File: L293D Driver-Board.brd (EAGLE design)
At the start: 62.2 x 47.9 mm, 13 parts, among them IC1 L293D, IC3 LM317MBSTT3

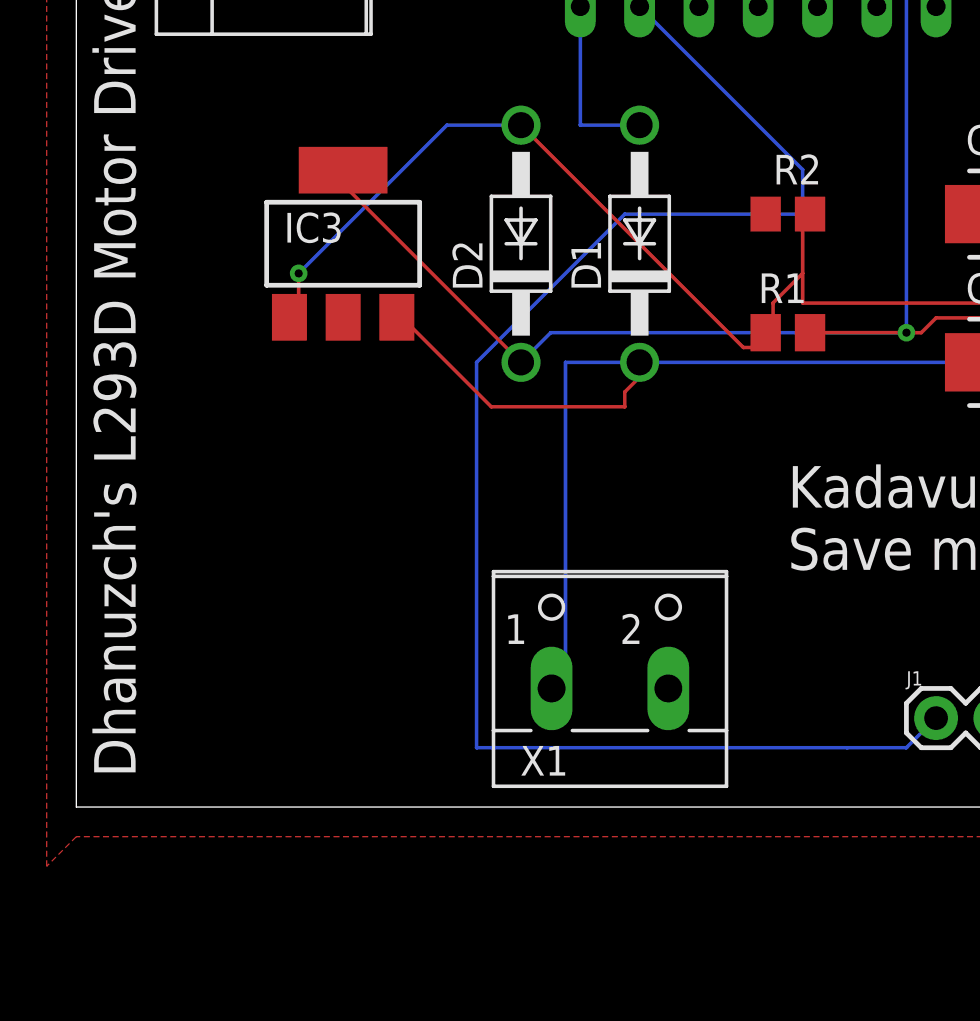
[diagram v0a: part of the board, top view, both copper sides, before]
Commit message: Changed Resistor Values
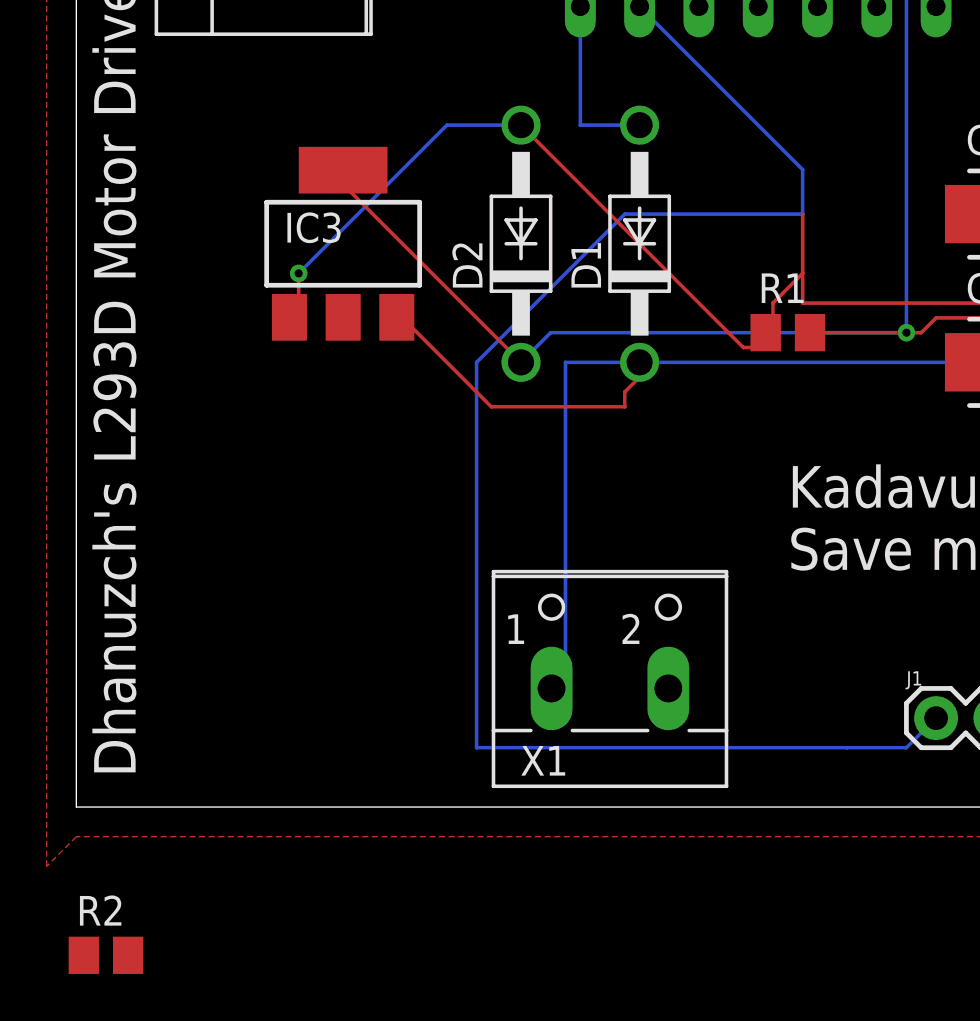
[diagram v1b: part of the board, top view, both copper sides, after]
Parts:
- R2: value (none) -> 720Ω; device designblock:R0805 -> resistor:M0805
- moved R2 43.1 mm to (1.27, -6.35)
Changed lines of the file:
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@@
 <attribute name="VALUE" x="29.21" y="17.78" size="1.27" layer="27"/>
-</element>
-<element name="R2" library="designblock" package="R0805" value="" x="30.48" y="25.4" smashed="yes">
-<attribute name="NAME" x="29.845" y="26.67" size="1.27" layer="25"/>
-<attribute name="VALUE" x="29.845" y="22.86" size="1.27" layer="27"/>
 </element>
 <element name="X1" library="con-wago-500" library_urn="urn:adsk.eagle:library:195" package="W237-102" package3d_urn="urn:adsk.eagle:package:10688/1" value="" x="22.86" y="6.35" smashed="yes">
@@
 <attribute name="VALUE" x="1.27" y="43.14" size="1.27" layer="27" ratio="10" rot="R270"/>
 </element>
+<element name="R2" library="resistor" library_urn="urn:adsk.eagle:library:348" package="M0805" package3d_urn="urn:adsk.eagle:package:26079/1" value="720Ω" x="1.27" y="-6.35" smashed="yes">
+<attribute name="NAME" x="0" y="-5.08" size="1.27" layer="25"/>
+<attribute name="VALUE" x="0" y="-8.89" size="1.27" layer="27"/>
+</element>
 </elements>
 <signals>
@@
 <contactref element="C3" pad="2"/>
 <contactref element="X1" pad="2"/>
-<contactref element="R2" pad="1"/>
 <contactref element="C5" pad="-"/>
 <contactref element="C4" pad="-"/>
@@
 <vertex x="-1.27" y="48.26"/>
 </polygon>
+<contactref element="R2" pad="1"/>
+<wire x1="38.66" y1="25.4" x2="52.07" y2="26.67" width="0" layer="19" extent="1-1"/>
+<wire x1="38.66" y1="19.05" x2="38.66" y2="25.4" width="0" layer="19" extent="1-1"/>
+<wire x1="31.75" y1="34.29" x2="38.66" y2="25.4" width="0" layer="19" extent="1-1"/>
+<wire x1="29.21" y1="34.29" x2="31.75" y2="34.29" width="0" layer="19" extent="1-1"/>
+<wire x1="31.75" y1="41.91" x2="31.75" y2="34.29" width="0" layer="19" extent="1-1"/>
+<wire x1="29.21" y1="41.91" x2="31.75" y2="41.91" width="0" layer="19" extent="1-1"/>
+<wire x1="25.36" y1="5.08" x2="38.66" y2="19.05" width="0" layer="19" extent="1-1"/>
+<wire x1="0.32" y1="-6.35" x2="25.36" y2="5.08" width="0" layer="19" extent="1-1"/>
 </signal>
 <signal name="N$1">
@@
 <contactref element="C5" pad="+"/>
 <contactref element="IC3" pad="1"/>
-<contactref element="R2" pad="2"/>
 <wire x1="9.525" y1="22.86" x2="9.525" y2="21.59" width="0.1524" layer="1"/>
 <wire x1="15.875" y1="29.21" x2="9.525" y2="22.86" width="0.1524" layer="16"/>
@@
 <wire x1="29.845" y1="21.59" x2="31.115" y2="22.86" width="0.1524" layer="1"/>
 <wire x1="29.845" y1="20.32" x2="29.845" y2="21.59" width="0.1524" layer="1"/>
-<wire x1="31.115" y1="25.4" x2="31.43" y2="25.4" width="0.1524" layer="1"/>
 <wire x1="29.845" y1="20.32" x2="29.53" y2="20.32" width="0.1524" layer="1"/>
 <wire x1="41.275" y1="21.59" x2="45.085" y2="25.4" width="0.1524" layer="1"/>
@@
 <wire x1="29.21" y1="20.32" x2="29.53" y2="20.32" width="0.1524" layer="1"/>
 <via x="9.525" y="22.86" extent="1-16" drill="0.35"/>
+<contactref element="R2" pad="2"/>
+<wire x1="2.22" y1="-6.35" x2="9.13" y2="20.98" width="0" layer="19" extent="1-1"/>
 </signal>
 <signal name="VO">
